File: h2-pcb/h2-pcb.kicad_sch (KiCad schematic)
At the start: 60 parts, among them J10 Temp Sensor Conn 3, J11 Actuator Connector 4, J12 Manometer Connector 3, J3 Manometer Connector 1, J4 Manometer Connector 2, J5 Actuator Connector 1, J6 Actuator Connector 2, J7 Actuator Connector 3, J8 Temp Sensor Conn 1, J9 Temp Sensor Conn 2, Q1 NMOS, Q2 PMOS, Q3 NMOS, Q4 PMOS, Q5 NMOS, Q6 PMOS, Q7 NMOS, Q8 PMOS, U4 DS2484

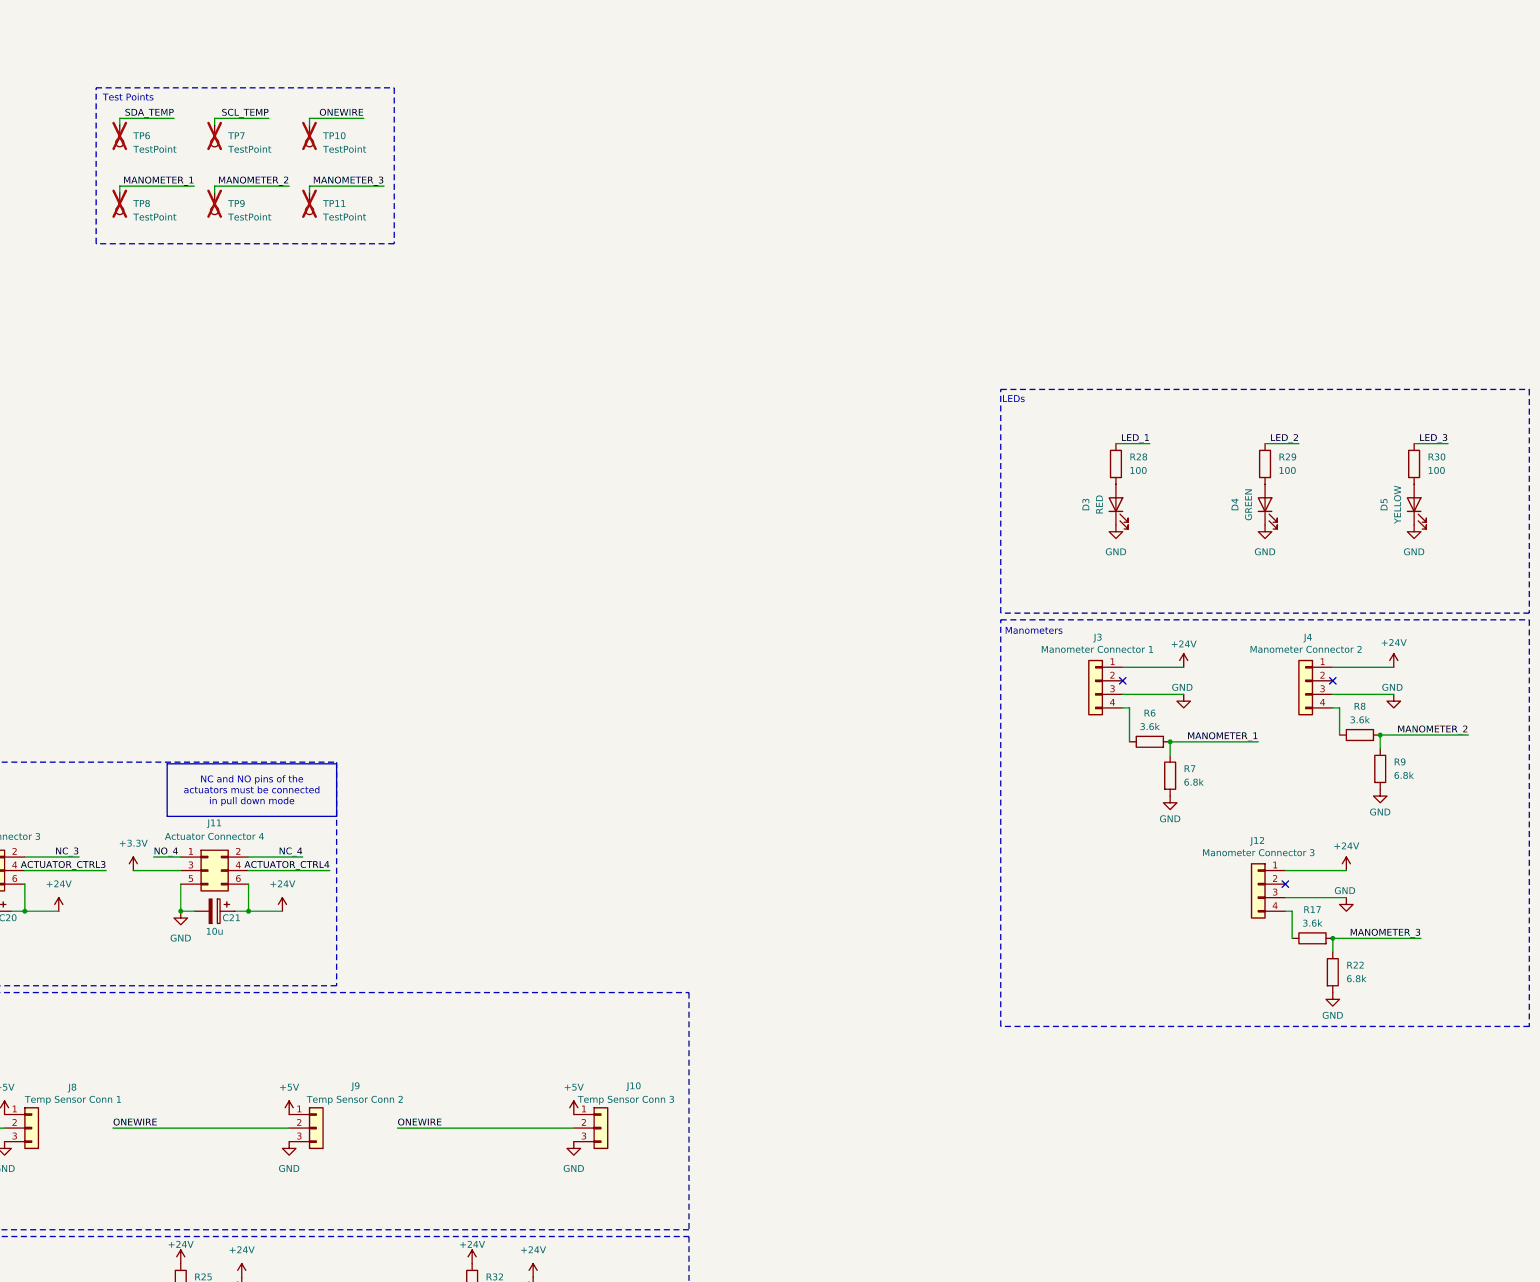
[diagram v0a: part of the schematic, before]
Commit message: Ajout des noms des composantes, routage des test points, 24V plane pour les manometres,  mounting holes 4mm de distance du edge
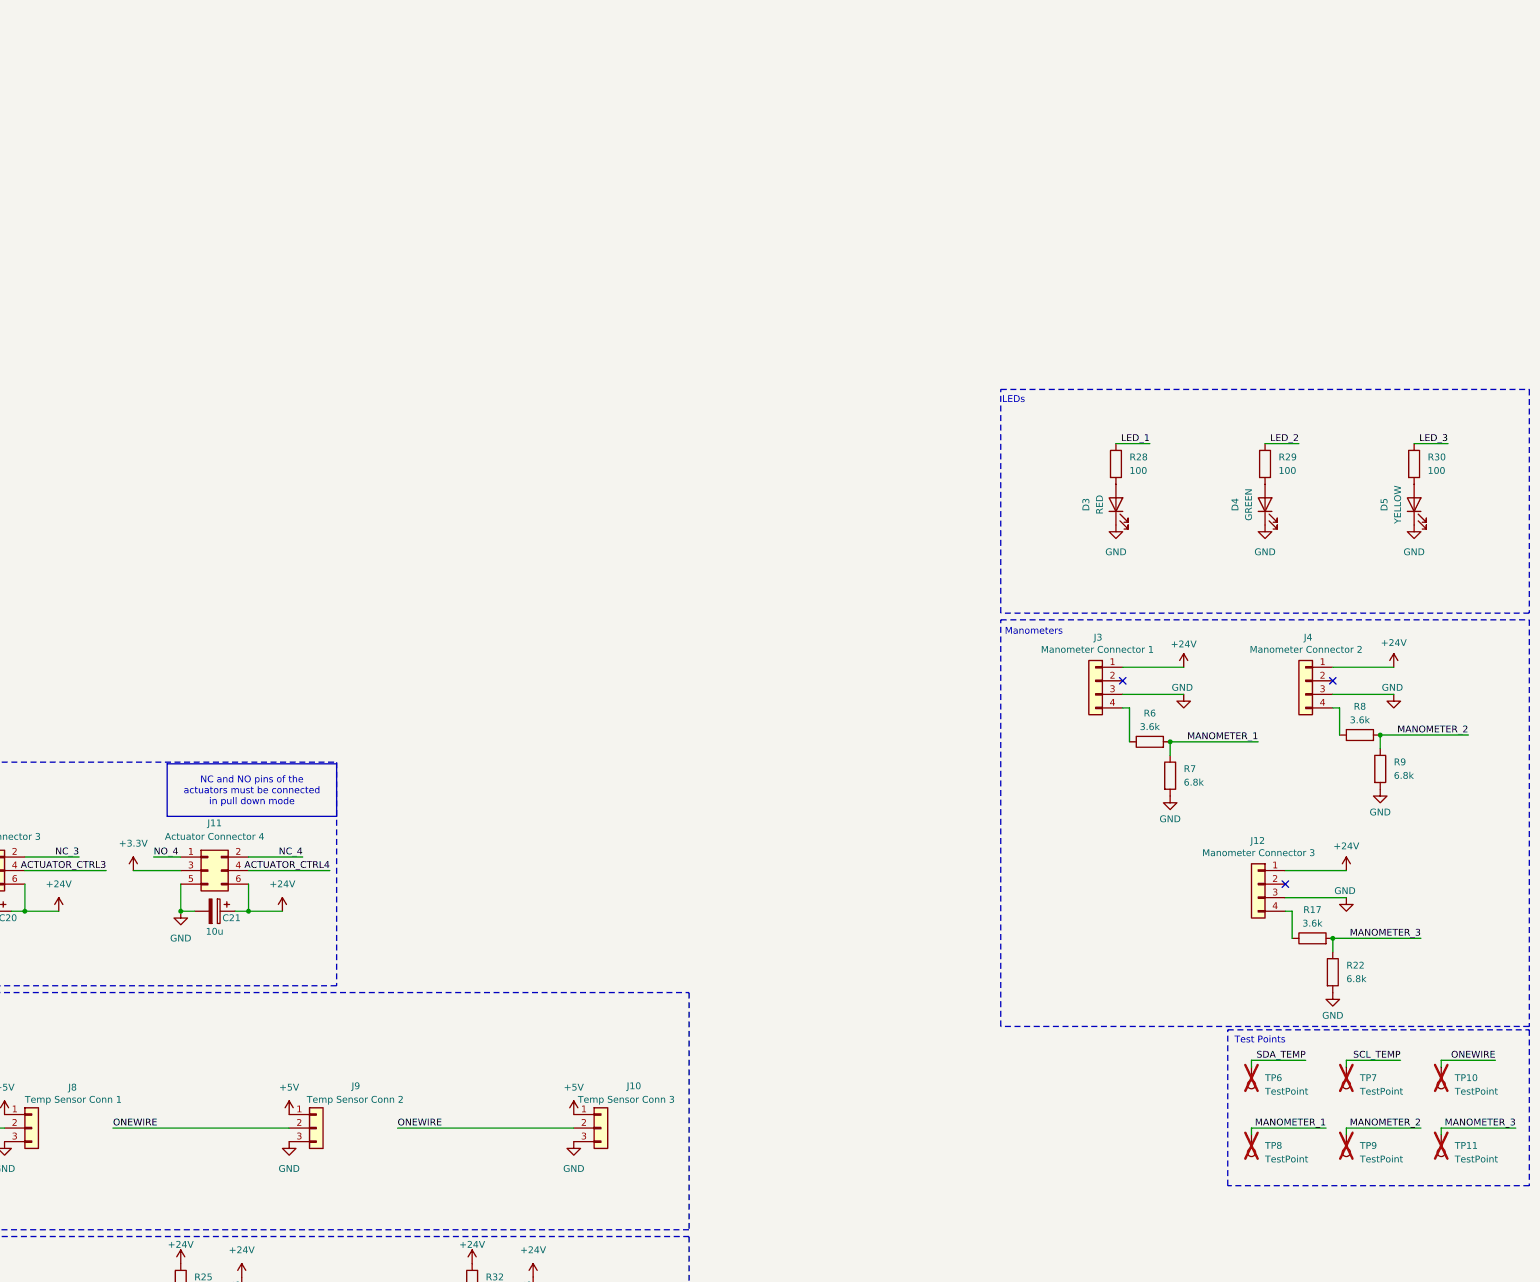
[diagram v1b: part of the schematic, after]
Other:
- moved on the sheet: TP10, TP11, TP6, TP7, TP8, TP9
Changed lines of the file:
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@@
 	)
 	(rectangle
-		(start 137.795 27.305)
-		(end 193.675 56.515)
+		(start 349.885 203.835)
+		(end 406.4 233.045)
 		(stroke
 			(width 0)
@@
 	(text "Test Points"
 		(exclude_from_sim no)
-		(at 139.065 28.575 0)
+		(at 351.155 205.105 0)
 		(effects
 			(font
@@
 	(wire
 		(pts
-			(xy 160.02 33.02) (xy 170.18 33.02)
+			(xy 372.11 209.55) (xy 382.27 209.55)
 		)
 		(stroke
@@
 	(wire
 		(pts
-			(xy 142.24 33.02) (xy 152.4 33.02)
+			(xy 354.33 209.55) (xy 364.49 209.55)
 		)
 		(stroke
@@
 	(wire
 		(pts
-			(xy 177.8 45.72) (xy 191.77 45.72)
+			(xy 389.89 222.25) (xy 403.86 222.25)
 		)
 		(stroke
@@
 	(wire
 		(pts
-			(xy 160.02 45.72) (xy 173.99 45.72)
+			(xy 372.11 222.25) (xy 386.08 222.25)
 		)
 		(stroke
@@
 	(wire
 		(pts
-			(xy 160.02 46.99) (xy 160.02 45.72)
+			(xy 372.11 223.52) (xy 372.11 222.25)
 		)
 		(stroke
@@
 	(wire
 		(pts
-			(xy 177.8 33.02) (xy 187.96 33.02)
+			(xy 389.89 209.55) (xy 400.05 209.55)
 		)
 		(stroke
@@
 	(wire
 		(pts
-			(xy 142.24 46.99) (xy 142.24 45.72)
+			(xy 354.33 223.52) (xy 354.33 222.25)
 		)
 		(stroke
@@
 	(wire
 		(pts
-			(xy 177.8 34.29) (xy 177.8 33.02)
+			(xy 389.89 210.82) (xy 389.89 209.55)
 		)
 		(stroke
@@
 	(wire
 		(pts
-			(xy 142.24 34.29) (xy 142.24 33.02)
+			(xy 354.33 210.82) (xy 354.33 209.55)
 		)
 		(stroke
@@
 	(wire
 		(pts
-			(xy 177.8 46.99) (xy 177.8 45.72)
+			(xy 389.89 223.52) (xy 389.89 222.25)
 		)
 		(stroke
@@
 	(wire
 		(pts
-			(xy 160.02 34.29) (xy 160.02 33.02)
+			(xy 372.11 210.82) (xy 372.11 209.55)
 		)
 		(stroke
@@
 	(wire
 		(pts
-			(xy 142.24 45.72) (xy 156.21 45.72)
+			(xy 354.33 222.25) (xy 368.3 222.25)
 		)
 		(stroke
@@
 	)
 	(label "SCL_TEMP"
-		(at 170.18 33.02 180)
+		(at 382.27 209.55 180)
 		(effects
 			(font
@@
 	)
 	(label "ONEWIRE"
-		(at 187.96 33.02 180)
+		(at 400.05 209.55 180)
 		(effects
 			(font
@@
 	)
 	(label "MANOMETER_1"
-		(at 156.21 45.72 180)
+		(at 368.3 222.25 180)
 		(effects
 			(font
@@
 	)
 	(label "SDA_TEMP"
-		(at 152.4 33.02 180)
+		(at 364.49 209.55 180)
 		(effects
 			(font
@@
 	)
 	(label "MANOMETER_3"
-		(at 191.77 45.72 180)
+		(at 403.86 222.25 180)
 		(effects
 			(font
@@
 	)
 	(label "MANOMETER_2"
-		(at 173.99 45.72 180)
+		(at 386.08 222.25 180)
 		(effects
 			(font
@@
 	(symbol
 		(lib_id "Connector:TestPoint")
-		(at 177.8 34.29 180)
+		(at 389.89 210.82 180)
 		(unit 1)
 		(exclude_from_sim no)
@@
 		(fields_autoplaced yes)
 		(property "Reference" "TP10"
-			(at 180.34 36.3219 0)
+			(at 392.43 212.8519 0)
 			(effects
 				(font
@@
 		)
 		(property "Value" "TestPoint"
-			(at 180.34 38.8619 0)
+			(at 392.43 215.3919 0)
 			(effects
 				(font
@@
 		)
 		(property "Footprint" "TestPoint:TestPoint_Keystone_5005-5009_Compact"
-			(at 172.72 34.29 0)
+			(at 384.81 210.82 0)
 			(effects
 				(font
@@
 		)
 		(property "Datasheet" "https://www.keyelco.com/userAssets/file/M65p56.pdf"
-			(at 172.72 34.29 0)
+			(at 384.81 210.82 0)
 			(effects
 				(font
@@
 		)
 		(property "Description" "test point"
-			(at 177.8 34.29 0)
+			(at 389.89 210.82 0)
 			(effects
 				(font
@@
 		)
 		(property "Net Label" "1-Wire"
-			(at 177.8 34.29 0)
+			(at 389.89 210.82 0)
 			(effects
 				(font
@@
 	(symbol
 		(lib_id "Connector:TestPoint")
-		(at 142.24 46.99 180)
+		(at 354.33 223.52 180)
 		(unit 1)
 		(exclude_from_sim no)
@@
 		(fields_autoplaced yes)
 		(property "Reference" "TP8"
-			(at 144.78 49.0219 0)
+			(at 356.87 225.5519 0)
 			(effects
 				(font
@@
 		)
 		(property "Value" "TestPoint"
-			(at 144.78 51.5619 0)
+			(at 356.87 228.0919 0)
 			(effects
 				(font
@@
 		)
 		(property "Footprint" "TestPoint:TestPoint_Keystone_5005-5009_Compact"
-			(at 137.16 46.99 0)
+			(at 349.25 223.52 0)
 			(effects
 				(font
@@
 		)
 		(property "Datasheet" "https://www.keyelco.com/userAssets/file/M65p56.pdf"
-			(at 137.16 46.99 0)
+			(at 349.25 223.52 0)
 			(effects
 				(font
@@
 		)
 		(property "Description" "test point"
-			(at 142.24 46.99 0)
+			(at 354.33 223.52 0)
 			(effects
 				(font
@@
 		)
 		(property "Net Label" "Man. 1"
-			(at 142.24 46.99 0)
+			(at 354.33 223.52 0)
 			(effects
 				(font
@@
 	(symbol
 		(lib_id "Connector:TestPoint")
-		(at 160.02 46.99 180)
+		(at 372.11 223.52 180)
 		(unit 1)
 		(exclude_from_sim no)
@@
 		(fields_autoplaced yes)
 		(property "Reference" "TP9"
-			(at 162.56 49.0219 0)
+			(at 374.65 225.5519 0)
 			(effects
 				(font
@@
 		)
 		(property "Value" "TestPoint"
-			(at 162.56 51.5619 0)
+			(at 374.65 228.0919 0)
 			(effects
 				(font
@@
 		)
 		(property "Footprint" "TestPoint:TestPoint_Keystone_5005-5009_Compact"
-			(at 154.94 46.99 0)
+			(at 367.03 223.52 0)
 			(effects
 				(font
@@
 		)
 		(property "Datasheet" "https://www.keyelco.com/userAssets/file/M65p56.pdf"
-			(at 154.94 46.99 0)
+			(at 367.03 223.52 0)
 			(effects
 				(font
@@
 		)
 		(property "Description" "test point"
-			(at 160.02 46.99 0)
+			(at 372.11 223.52 0)
 			(effects
 				(font
@@
 		)
 		(property "Net Label" "Man. 2"
-			(at 160.02 46.99 0)
+			(at 372.11 223.52 0)
 			(effects
 				(font
@@
 	(symbol
 		(lib_id "Connector:TestPoint")
-		(at 160.02 34.29 180)
+		(at 372.11 210.82 180)
 		(unit 1)
 		(exclude_from_sim no)
@@
 		(fields_autoplaced yes)
 		(property "Reference" "TP7"
-			(at 162.56 36.3219 0)
+			(at 374.65 212.8519 0)
 			(effects
 				(font
@@
 		)
 		(property "Value" "TestPoint"
-			(at 162.56 38.8619 0)
+			(at 374.65 215.3919 0)
 			(effects
 				(font
@@
 		)
 		(property "Footprint" "TestPoint:TestPoint_Keystone_5005-5009_Compact"
-			(at 154.94 34.29 0)
+			(at 367.03 210.82 0)
 			(effects
 				(font
@@
 		)
 		(property "Datasheet" "https://www.keyelco.com/userAssets/file/M65p56.pdf"
-			(at 154.94 34.29 0)
+			(at 367.03 210.82 0)
 			(effects
 				(font
@@
 		)
 		(property "Description" "test point"
-			(at 160.02 34.29 0)
+			(at 372.11 210.82 0)
 			(effects
 				(font
@@
 		)
 		(property "Net Label" "SCL"
-			(at 160.02 34.29 0)
+			(at 372.11 210.82 0)
 			(effects
 				(font
@@
 	(symbol
 		(lib_id "Connector:TestPoint")
-		(at 177.8 46.99 180)
+		(at 389.89 223.52 180)
 		(unit 1)
 		(exclude_from_sim no)
@@
 		(fields_autoplaced yes)
 		(property "Reference" "TP11"
-			(at 180.34 49.0219 0)
+			(at 392.43 225.5519 0)
 			(effects
 				(font
@@
 		)
 		(property "Value" "TestPoint"
-			(at 180.34 51.5619 0)
+			(at 392.43 228.0919 0)
 			(effects
 				(font
@@
 		)
 		(property "Footprint" "TestPoint:TestPoint_Keystone_5005-5009_Compact"
-			(at 172.72 46.99 0)
+			(at 384.81 223.52 0)
 			(effects
 				(font
@@
 		)
 		(property "Datasheet" "https://www.keyelco.com/userAssets/file/M65p56.pdf"
-			(at 172.72 46.99 0)
+			(at 384.81 223.52 0)
 			(effects
 				(font
@@
 		)
 		(property "Description" "test point"
-			(at 177.8 46.99 0)
+			(at 389.89 223.52 0)
 			(effects
 				(font
@@
 		)
 		(property "Net Label" "Man. 3"
-			(at 177.8 46.99 0)
+			(at 389.89 223.52 0)
 			(effects
 				(font
@@
 	(symbol
 		(lib_id "Connector:TestPoint")
-		(at 142.24 34.29 180)
+		(at 354.33 210.82 180)
 		(unit 1)
 		(exclude_from_sim no)
@@
 		(fields_autoplaced yes)
 		(property "Reference" "TP6"
-			(at 144.78 36.3219 0)
+			(at 356.87 212.8519 0)
 			(effects
 				(font
@@
 		)
 		(property "Value" "TestPoint"
-			(at 144.78 38.8619 0)
+			(at 356.87 215.3919 0)
 			(effects
 				(font
@@
 		)
 		(property "Footprint" "TestPoint:TestPoint_Keystone_5005-5009_Compact"
-			(at 137.16 34.29 0)
+			(at 349.25 210.82 0)
 			(effects
 				(font
@@
 		)
 		(property "Datasheet" "https://www.keyelco.com/userAssets/file/M65p56.pdf"
-			(at 137.16 34.29 0)
+			(at 349.25 210.82 0)
 			(effects
 				(font
@@
 		)
 		(property "Description" "test point"
-			(at 142.24 34.29 0)
+			(at 354.33 210.82 0)
 			(effects
 				(font
@@
 		)
 		(property "Net Label" "SDA"
-			(at 142.24 34.29 0)
+			(at 354.33 210.82 0)
 			(effects
 				(font

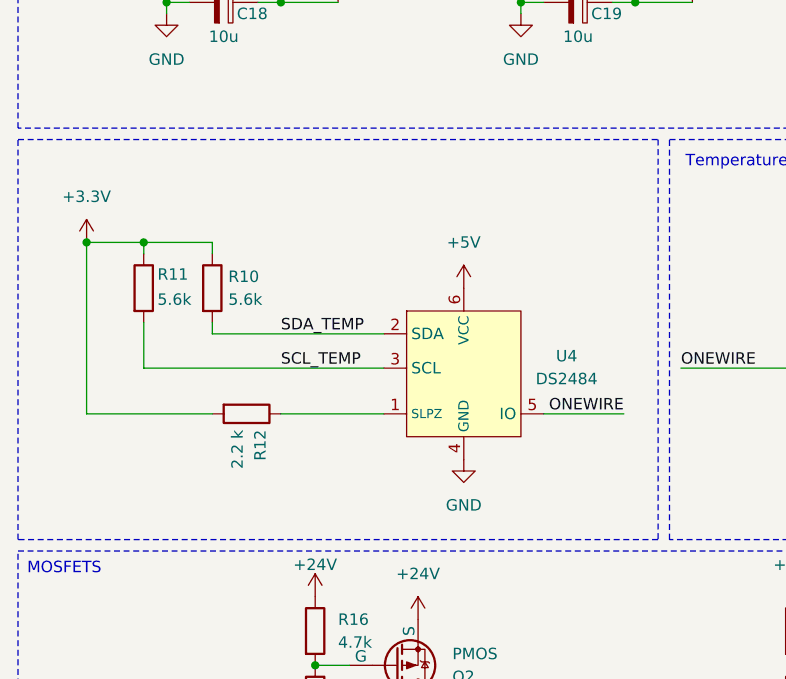
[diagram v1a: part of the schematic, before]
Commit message: h2-pcb: replace ds2484 symbol
The symbol is now the one from the official KiCad library. PCB was also
updated and any remaining DRC errors were fixed.
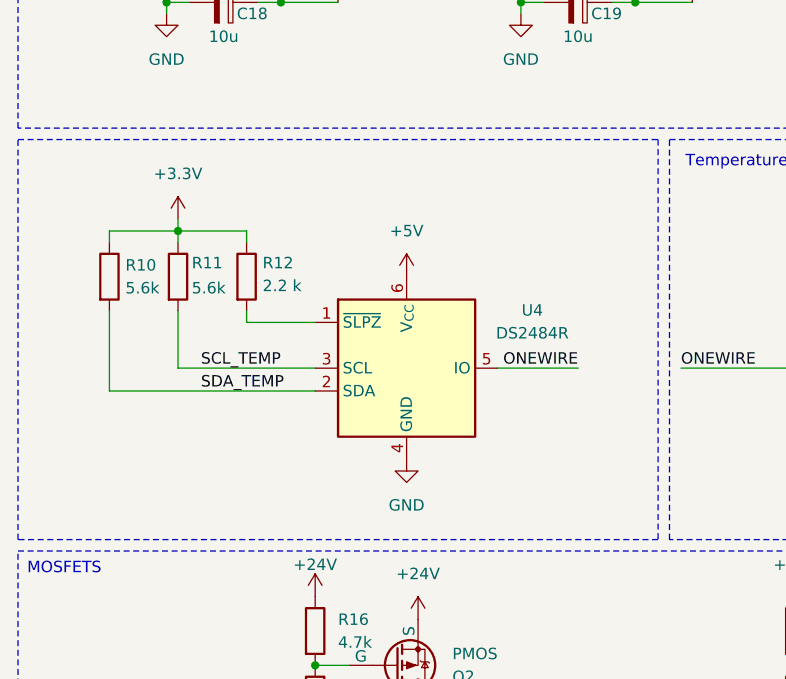
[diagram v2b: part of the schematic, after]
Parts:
- removed U4: DS2484, Package_DFN_QFN:TDFN-8-1EP_3x2mm_P0.5mm_EP1.4x1.4mm, symbol Exocet:DS2482-100
- added U4: DS2484R, Package_TO_SOT_SMD:SOT-23-6, symbol Interface_Expansion:DS2484R
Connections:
- net +3.3V: now also R12.1; no longer R12.2
- net +5V: now also U4.6 (V_{CC})
- net GND: now also U4.4 (GND)
- net ONEWIRE: now also U4.5 (IO)
- net SCL_TEMP: now also U4.3 (SCL)
- net SDA_TEMP: now also U4.2 (SDA)
- new net: R12.2, U4.1 (~{SLPZ})
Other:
- moved on the sheet: R10, R11, R12
